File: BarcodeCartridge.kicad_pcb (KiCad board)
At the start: 2 copper layers, 64.8 x 55.9 mm, 3 parts, among them J1 Cartridge Connector, U1 W25Q128

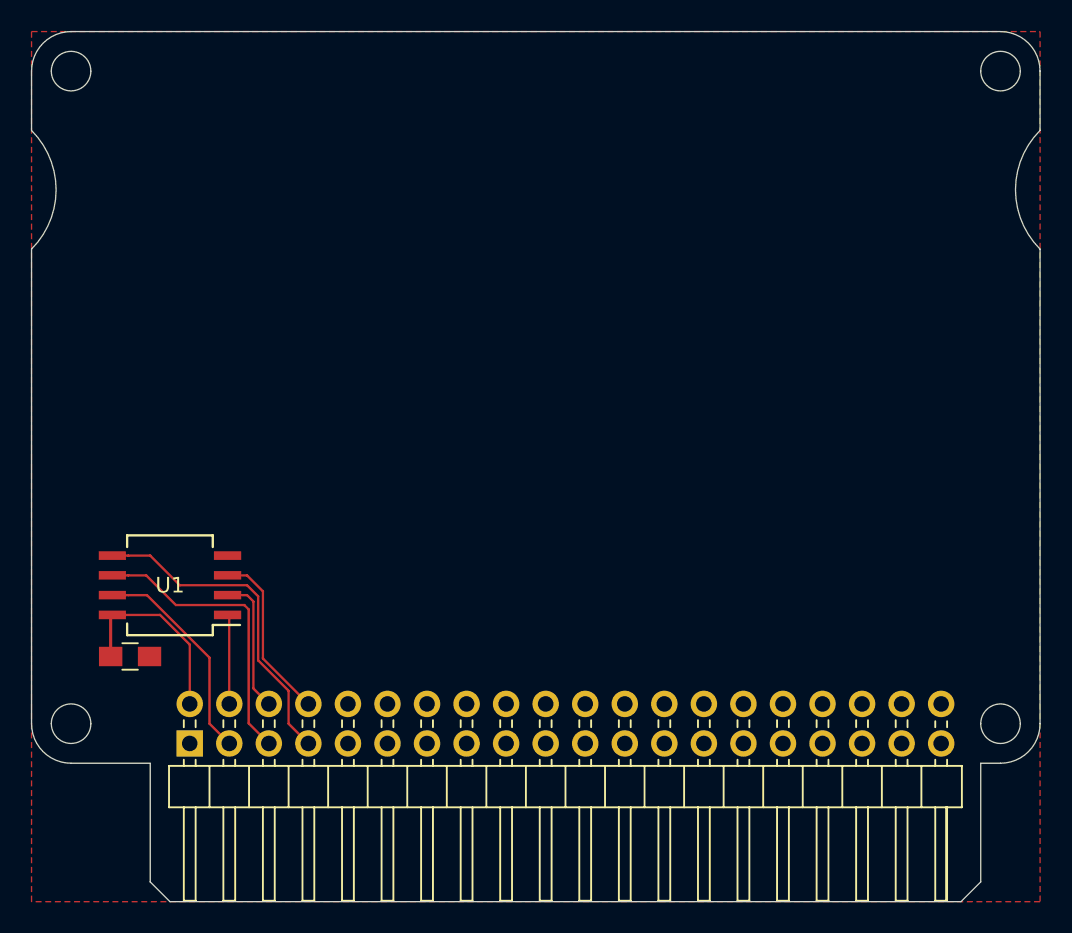
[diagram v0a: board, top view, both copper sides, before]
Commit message: First design of the Barcode reader cartridge
Also updated:
- README
- Render image
- .gitignore
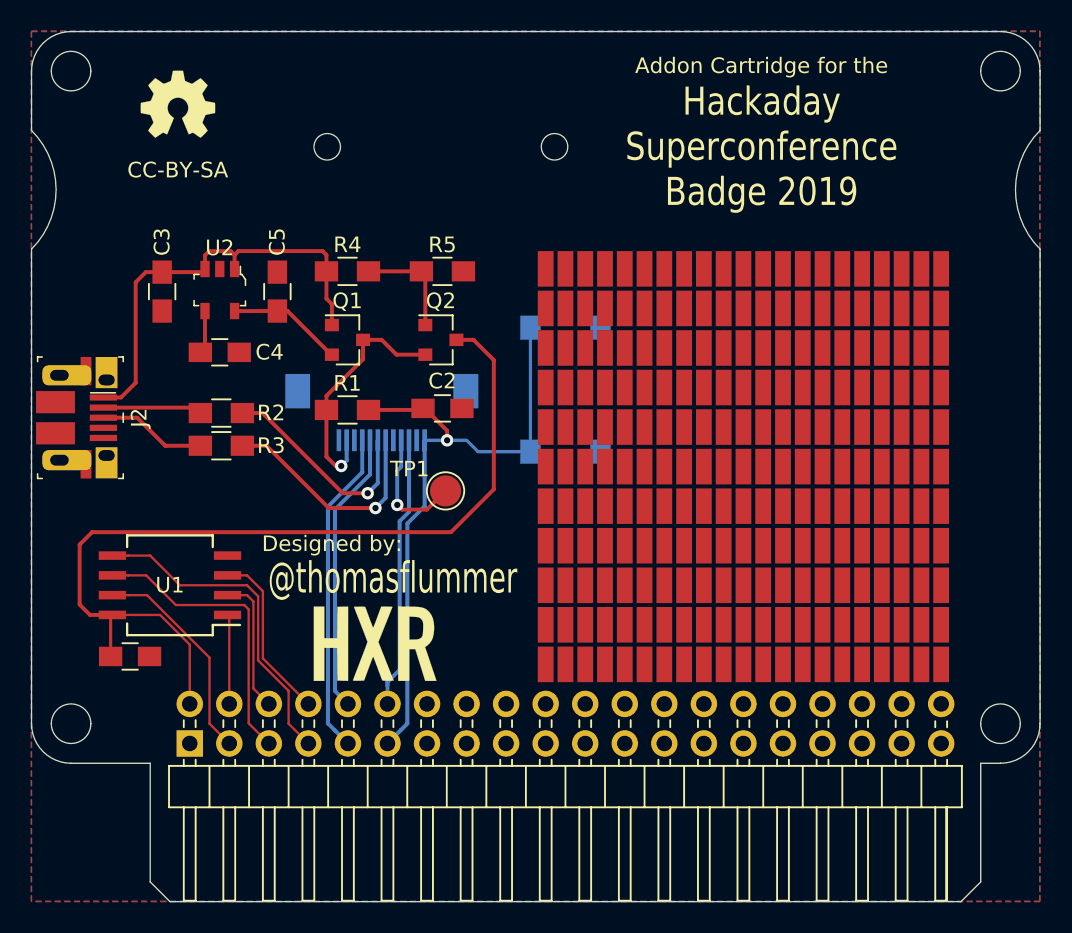
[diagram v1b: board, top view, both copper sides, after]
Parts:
- added C2: 0.1uF, Capacitors_SMD:C_0805_HandSoldering, F.Cu at (93.7, 75.0)
- added C3: 1uF, Capacitors_SMD:C_0805_HandSoldering, F.Cu at (75.7, 67.5)
- added C4: 0.1uF, Capacitors_SMD:C_0805_HandSoldering, F.Cu at (79.4, 71.4)
- added C5: 2.2uF, Capacitors_SMD:C_0805_HandSoldering, F.Cu at (83.1, 67.5)
- added G***: LOGO, Aesthetics:oshw_logo_5.0mm, F.Cu at (76.7, 55.5)
- added G***: LOGO, Aesthetics:HXR_logo_small, F.Cu at (92.1, 90.1)
- added J2: 10103594-0001LF, digikey-footprints:USB_Micro_B_Female_10103594-0001LF, F.Cu at (69.1, 75.6)
- added M1: GM65-S, SuperconCartridge:SD-52892-044, B.Cu at (89.8, 75.0)
- added Q1: SMD-MOSFET-N-CH-20V-2.1A-CJ2302_SOT-23_, TO_SOT_Packages_SMD:SOT-23, F.Cu at (87.6, 70.6)
- added Q2: SMD-MOSFET-P-CH-8V-4.1A-CJ2305_SOT-23_, TO_SOT_Packages_SMD:SOT-23, F.Cu at (93.6, 70.6)
- added R1: 4.7k, Resistors_SMD:R_0805_HandSoldering, F.Cu at (87.6, 75.1)
- added R2: 22, Resistors_SMD:R_0805_HandSoldering, F.Cu at (79.5, 75.3)
- added R3: 22, Resistors_SMD:R_0805_HandSoldering, F.Cu at (79.5, 77.4)
- added R4: 4.7k, Resistors_SMD:R_0805_HandSoldering, F.Cu at (87.6, 66.2)
- added R5: 6.8k, Resistors_SMD:R_0805_HandSoldering, F.Cu at (93.7, 66.2)
- added READER MODULE: GM65-S, SuperconCartridge:GM65-S, B.Cu at (93.6, 50.8)
- added REF**: SMD Proto pad, Connectors:SMD_Proto_pad, F.Cu at (124.5, 66.0)
- added REF**: SMD Proto pad, Connectors:SMD_Proto_pad, F.Cu at (102.9, 66.0)
- added REF**: SMD Proto pad, Connectors:SMD_Proto_pad, F.Cu at (121.9, 76.2)
- added REF**: SMD Proto pad, Connectors:SMD_Proto_pad, F.Cu at (108.0, 76.2)
- added REF**: SMD Proto pad, Connectors:SMD_Proto_pad, F.Cu at (101.6, 76.2)
- added REF**: SMD Proto pad, Connectors:SMD_Proto_pad, F.Cu at (118.1, 76.2)
- added REF**: SMD Proto pad, Connectors:SMD_Proto_pad, F.Cu at (125.7, 76.2)
- added REF**: SMD Proto pad, Connectors:SMD_Proto_pad, F.Cu at (123.2, 76.2)
- added REF**: SMD Proto pad, Connectors:SMD_Proto_pad, F.Cu at (124.5, 78.7)
- added REF**: SMD Proto pad, Connectors:SMD_Proto_pad, F.Cu at (105.4, 78.7)
- added REF**: SMD Proto pad, Connectors:SMD_Proto_pad, F.Cu at (100.3, 78.7)
- added REF**: SMD Proto pad, Connectors:SMD_Proto_pad, F.Cu at (116.8, 78.7)
- added REF**: SMD Proto pad, Connectors:SMD_Proto_pad, F.Cu at (111.8, 66.0)
- added REF**: SMD Proto pad, Connectors:SMD_Proto_pad, F.Cu at (102.9, 78.7)
- added REF**: SMD Proto pad, Connectors:SMD_Proto_pad, F.Cu at (114.3, 78.7)
- added REF**: SMD Proto pad, Connectors:SMD_Proto_pad, F.Cu at (104.1, 78.7)
- added REF**: SMD Proto pad, Connectors:SMD_Proto_pad, F.Cu at (106.7, 78.7)
- added REF**: SMD Proto pad, Connectors:SMD_Proto_pad, F.Cu at (113.0, 78.7)
- added REF**: SMD Proto pad, Connectors:SMD_Proto_pad, F.Cu at (119.4, 78.7)
- added REF**: SMD Proto pad, Connectors:SMD_Proto_pad, F.Cu at (120.7, 78.7)
- added REF**: SMD Proto pad, Connectors:SMD_Proto_pad, F.Cu at (115.6, 78.7)
- added REF**: SMD Proto pad, Connectors:SMD_Proto_pad, F.Cu at (110.5, 78.7)
- added REF**: SMD Proto pad, Connectors:SMD_Proto_pad, F.Cu at (111.8, 78.7)
- added REF**: SMD Proto pad, Connectors:SMD_Proto_pad, F.Cu at (109.2, 66.0)
- added REF**: SMD Proto pad, Connectors:SMD_Proto_pad, F.Cu at (109.2, 78.7)
- added REF**: SMD Proto pad, Connectors:SMD_Proto_pad, F.Cu at (121.9, 78.7)
- added REF**: SMD Proto pad, Connectors:SMD_Proto_pad, F.Cu at (108.0, 78.7)
- added REF**: SMD Proto pad, Connectors:SMD_Proto_pad, F.Cu at (101.6, 78.7)
- added REF**: SMD Proto pad, Connectors:SMD_Proto_pad, F.Cu at (118.1, 78.7)
- added REF**: SMD Proto pad, Connectors:SMD_Proto_pad, F.Cu at (125.7, 78.7)
- added REF**: SMD Proto pad, Connectors:SMD_Proto_pad, F.Cu at (123.2, 78.7)
- added REF**: SMD Proto pad, Connectors:SMD_Proto_pad, F.Cu at (124.5, 81.3)
- added REF**: SMD Proto pad, Connectors:SMD_Proto_pad, F.Cu at (105.4, 81.3)
- added REF**: SMD Proto pad, Connectors:SMD_Proto_pad, F.Cu at (100.3, 81.3)
- added REF**: SMD Proto pad, Connectors:SMD_Proto_pad, F.Cu at (114.3, 66.0)
- added REF**: SMD Proto pad, Connectors:SMD_Proto_pad, F.Cu at (116.8, 81.3)
- added REF**: SMD Proto pad, Connectors:SMD_Proto_pad, F.Cu at (102.9, 81.3)
- added REF**: SMD Proto pad, Connectors:SMD_Proto_pad, F.Cu at (114.3, 81.3)
- added REF**: SMD Proto pad, Connectors:SMD_Proto_pad, F.Cu at (104.1, 81.3)
- added REF**: SMD Proto pad, Connectors:SMD_Proto_pad, F.Cu at (106.7, 81.3)
- added REF**: SMD Proto pad, Connectors:SMD_Proto_pad, F.Cu at (113.0, 81.3)
- added REF**: SMD Proto pad, Connectors:SMD_Proto_pad, F.Cu at (119.4, 81.3)
- added REF**: SMD Proto pad, Connectors:SMD_Proto_pad, F.Cu at (120.7, 81.3)
- added REF**: SMD Proto pad, Connectors:SMD_Proto_pad, F.Cu at (115.6, 81.3)
- added REF**: SMD Proto pad, Connectors:SMD_Proto_pad, F.Cu at (110.5, 81.3)
- added REF**: SMD Proto pad, Connectors:SMD_Proto_pad, F.Cu at (104.1, 66.0)
- added REF**: SMD Proto pad, Connectors:SMD_Proto_pad, F.Cu at (111.8, 81.3)
- added REF**: SMD Proto pad, Connectors:SMD_Proto_pad, F.Cu at (109.2, 81.3)
- added REF**: SMD Proto pad, Connectors:SMD_Proto_pad, F.Cu at (121.9, 81.3)
- added REF**: SMD Proto pad, Connectors:SMD_Proto_pad, F.Cu at (108.0, 81.3)
- added REF**: SMD Proto pad, Connectors:SMD_Proto_pad, F.Cu at (101.6, 81.3)
- added REF**: SMD Proto pad, Connectors:SMD_Proto_pad, F.Cu at (118.1, 81.3)
- added REF**: SMD Proto pad, Connectors:SMD_Proto_pad, F.Cu at (125.7, 81.3)
- added REF**: SMD Proto pad, Connectors:SMD_Proto_pad, F.Cu at (123.2, 81.3)
- added REF**: SMD Proto pad, Connectors:SMD_Proto_pad, F.Cu at (123.2, 83.8)
- added REF**: SMD Proto pad, Connectors:SMD_Proto_pad, F.Cu at (118.1, 83.8)
- added REF**: SMD Proto pad, Connectors:SMD_Proto_pad, F.Cu at (106.7, 66.0)
- added REF**: SMD Proto pad, Connectors:SMD_Proto_pad, F.Cu at (125.7, 83.8)
- added REF**: SMD Proto pad, Connectors:SMD_Proto_pad, F.Cu at (120.7, 83.8)
- added REF**: SMD Proto pad, Connectors:SMD_Proto_pad, F.Cu at (115.6, 83.8)
- added REF**: SMD Proto pad, Connectors:SMD_Proto_pad, F.Cu at (110.5, 83.8)
- added REF**: SMD Proto pad, Connectors:SMD_Proto_pad, F.Cu at (111.8, 83.8)
- added REF**: SMD Proto pad, Connectors:SMD_Proto_pad, F.Cu at (109.2, 83.8)
- added REF**: SMD Proto pad, Connectors:SMD_Proto_pad, F.Cu at (119.4, 83.8)
- added REF**: SMD Proto pad, Connectors:SMD_Proto_pad, F.Cu at (104.1, 83.8)
- added REF**: SMD Proto pad, Connectors:SMD_Proto_pad, F.Cu at (106.7, 83.8)
- added REF**: SMD Proto pad, Connectors:SMD_Proto_pad, F.Cu at (113.0, 83.8)
- added REF**: SMD Proto pad, Connectors:SMD_Proto_pad, F.Cu at (113.0, 66.0)
- added REF**: SMD Proto pad, Connectors:SMD_Proto_pad, F.Cu at (100.3, 83.8)
- added REF**: SMD Proto pad, Connectors:SMD_Proto_pad, F.Cu at (116.8, 83.8)
- added REF**: SMD Proto pad, Connectors:SMD_Proto_pad, F.Cu at (102.9, 83.8)
- added REF**: SMD Proto pad, Connectors:SMD_Proto_pad, F.Cu at (114.3, 83.8)
- added REF**: SMD Proto pad, Connectors:SMD_Proto_pad, F.Cu at (124.5, 83.8)
- added REF**: SMD Proto pad, Connectors:SMD_Proto_pad, F.Cu at (105.4, 83.8)
- added REF**: SMD Proto pad, Connectors:SMD_Proto_pad, F.Cu at (121.9, 83.8)
- added REF**: SMD Proto pad, Connectors:SMD_Proto_pad, F.Cu at (108.0, 83.8)
- added REF**: SMD Proto pad, Connectors:SMD_Proto_pad, F.Cu at (101.6, 83.8)
- added REF**: SMD Proto pad, Connectors:SMD_Proto_pad, F.Cu at (123.2, 86.4)
- added REF**: SMD Proto pad, Connectors:SMD_Proto_pad, F.Cu at (119.4, 66.0)
- added REF**: SMD Proto pad, Connectors:SMD_Proto_pad, F.Cu at (108.0, 86.4)
- added REF**: SMD Proto pad, Connectors:SMD_Proto_pad, F.Cu at (116.8, 86.4)
- added REF**: SMD Proto pad, Connectors:SMD_Proto_pad, F.Cu at (104.1, 86.4)
- added REF**: SMD Proto pad, Connectors:SMD_Proto_pad, F.Cu at (106.7, 86.4)
- added REF**: SMD Proto pad, Connectors:SMD_Proto_pad, F.Cu at (113.0, 86.4)
- added REF**: SMD Proto pad, Connectors:SMD_Proto_pad, F.Cu at (100.3, 86.4)
- added REF**: SMD Proto pad, Connectors:SMD_Proto_pad, F.Cu at (102.9, 86.4)
- added REF**: SMD Proto pad, Connectors:SMD_Proto_pad, F.Cu at (114.3, 86.4)
- added REF**: SMD Proto pad, Connectors:SMD_Proto_pad, F.Cu at (124.5, 86.4)
- added REF**: SMD Proto pad, Connectors:SMD_Proto_pad, F.Cu at (105.4, 86.4)
- added REF**: SMD Proto pad, Connectors:SMD_Proto_pad, F.Cu at (120.7, 66.0)
- added REF**: SMD Proto pad, Connectors:SMD_Proto_pad, F.Cu at (118.1, 86.4)
- added REF**: SMD Proto pad, Connectors:SMD_Proto_pad, F.Cu at (125.7, 86.4)
- added REF**: SMD Proto pad, Connectors:SMD_Proto_pad, F.Cu at (120.7, 86.4)
- added REF**: SMD Proto pad, Connectors:SMD_Proto_pad, F.Cu at (115.6, 86.4)
- added REF**: SMD Proto pad, Connectors:SMD_Proto_pad, F.Cu at (121.9, 86.4)
- added REF**: SMD Proto pad, Connectors:SMD_Proto_pad, F.Cu at (110.5, 86.4)
- added REF**: SMD Proto pad, Connectors:SMD_Proto_pad, F.Cu at (111.8, 86.4)
- added REF**: SMD Proto pad, Connectors:SMD_Proto_pad, F.Cu at (109.2, 86.4)
- added REF**: SMD Proto pad, Connectors:SMD_Proto_pad, F.Cu at (119.4, 86.4)
- added REF**: SMD Proto pad, Connectors:SMD_Proto_pad, F.Cu at (101.6, 86.4)
- added REF**: SMD Proto pad, Connectors:SMD_Proto_pad, F.Cu at (115.6, 66.0)
- added REF**: SMD Proto pad, Connectors:SMD_Proto_pad, F.Cu at (110.5, 88.9)
- added REF**: SMD Proto pad, Connectors:SMD_Proto_pad, F.Cu at (125.7, 88.9)
- added REF**: SMD Proto pad, Connectors:SMD_Proto_pad, F.Cu at (120.7, 88.9)
- added REF**: SMD Proto pad, Connectors:SMD_Proto_pad, F.Cu at (115.6, 88.9)
- added REF**: SMD Proto pad, Connectors:SMD_Proto_pad, F.Cu at (111.8, 88.9)
- added REF**: SMD Proto pad, Connectors:SMD_Proto_pad, F.Cu at (121.9, 88.9)
- added REF**: SMD Proto pad, Connectors:SMD_Proto_pad, F.Cu at (123.2, 88.9)
- added REF**: SMD Proto pad, Connectors:SMD_Proto_pad, F.Cu at (114.3, 88.9)
- added REF**: SMD Proto pad, Connectors:SMD_Proto_pad, F.Cu at (102.9, 88.9)
- added REF**: SMD Proto pad, Connectors:SMD_Proto_pad, F.Cu at (108.0, 88.9)
- added REF**: SMD Proto pad, Connectors:SMD_Proto_pad, F.Cu at (105.4, 66.0)
- added REF**: SMD Proto pad, Connectors:SMD_Proto_pad, F.Cu at (110.5, 66.0)
- added REF**: SMD Proto pad, Connectors:SMD_Proto_pad, F.Cu at (116.8, 88.9)
- added REF**: SMD Proto pad, Connectors:SMD_Proto_pad, F.Cu at (104.1, 88.9)
- added REF**: SMD Proto pad, Connectors:SMD_Proto_pad, F.Cu at (106.7, 88.9)
- added REF**: SMD Proto pad, Connectors:SMD_Proto_pad, F.Cu at (113.0, 88.9)
- added REF**: SMD Proto pad, Connectors:SMD_Proto_pad, F.Cu at (100.3, 88.9)
- added REF**: SMD Proto pad, Connectors:SMD_Proto_pad, F.Cu at (119.4, 88.9)
- added REF**: SMD Proto pad, Connectors:SMD_Proto_pad, F.Cu at (101.6, 88.9)
- added REF**: SMD Proto pad, Connectors:SMD_Proto_pad, F.Cu at (109.2, 88.9)
- added REF**: SMD Proto pad, Connectors:SMD_Proto_pad, F.Cu at (105.4, 88.9)
- added REF**: SMD Proto pad, Connectors:SMD_Proto_pad, F.Cu at (118.1, 88.9)
- added REF**: SMD Proto pad, Connectors:SMD_Proto_pad, F.Cu at (123.2, 66.0)
- added REF**: SMD Proto pad, Connectors:SMD_Proto_pad, F.Cu at (124.5, 88.9)
- added REF**: SMD Proto pad, Connectors:SMD_Proto_pad, F.Cu at (125.7, 91.4)
- added REF**: SMD Proto pad, Connectors:SMD_Proto_pad, F.Cu at (124.5, 91.4)
- added REF**: SMD Proto pad, Connectors:SMD_Proto_pad, F.Cu at (123.2, 91.4)
- added REF**: SMD Proto pad, Connectors:SMD_Proto_pad, F.Cu at (121.9, 91.4)
- added REF**: SMD Proto pad, Connectors:SMD_Proto_pad, F.Cu at (120.7, 91.4)
- added REF**: SMD Proto pad, Connectors:SMD_Proto_pad, F.Cu at (119.4, 91.4)
- added REF**: SMD Proto pad, Connectors:SMD_Proto_pad, F.Cu at (118.1, 91.4)
- added REF**: SMD Proto pad, Connectors:SMD_Proto_pad, F.Cu at (116.8, 91.4)
- added REF**: SMD Proto pad, Connectors:SMD_Proto_pad, F.Cu at (115.6, 91.4)
- added REF**: SMD Proto pad, Connectors:SMD_Proto_pad, F.Cu at (124.5, 68.6)
- added REF**: SMD Proto pad, Connectors:SMD_Proto_pad, F.Cu at (114.3, 91.4)
- added REF**: SMD Proto pad, Connectors:SMD_Proto_pad, F.Cu at (113.0, 91.4)
- added REF**: SMD Proto pad, Connectors:SMD_Proto_pad, F.Cu at (111.8, 91.4)
- added REF**: SMD Proto pad, Connectors:SMD_Proto_pad, F.Cu at (110.5, 91.4)
- added REF**: SMD Proto pad, Connectors:SMD_Proto_pad, F.Cu at (109.2, 91.4)
- added REF**: SMD Proto pad, Connectors:SMD_Proto_pad, F.Cu at (108.0, 91.4)
- added REF**: SMD Proto pad, Connectors:SMD_Proto_pad, F.Cu at (106.7, 91.4)
- added REF**: SMD Proto pad, Connectors:SMD_Proto_pad, F.Cu at (105.4, 91.4)
- added REF**: SMD Proto pad, Connectors:SMD_Proto_pad, F.Cu at (104.1, 91.4)
- added REF**: SMD Proto pad, Connectors:SMD_Proto_pad, F.Cu at (102.9, 91.4)
- added REF**: SMD Proto pad, Connectors:SMD_Proto_pad, F.Cu at (105.4, 68.6)
- added REF**: SMD Proto pad, Connectors:SMD_Proto_pad, F.Cu at (101.6, 91.4)
- added REF**: SMD Proto pad, Connectors:SMD_Proto_pad, F.Cu at (100.3, 91.4)
- added REF**: SMD Proto pad, Connectors:SMD_Proto_pad, F.Cu at (121.9, 68.6)
- added REF**: SMD Proto pad, Connectors:SMD_Proto_pad, F.Cu at (108.0, 68.6)
- added REF**: SMD Proto pad, Connectors:SMD_Proto_pad, F.Cu at (101.6, 68.6)
- added REF**: SMD Proto pad, Connectors:SMD_Proto_pad, F.Cu at (118.1, 68.6)
- added REF**: SMD Proto pad, Connectors:SMD_Proto_pad, F.Cu at (125.7, 68.6)
- added REF**: SMD Proto pad, Connectors:SMD_Proto_pad, F.Cu at (100.3, 68.6)
- added REF**: SMD Proto pad, Connectors:SMD_Proto_pad, F.Cu at (121.9, 66.0)
- added REF**: SMD Proto pad, Connectors:SMD_Proto_pad, F.Cu at (116.8, 68.6)
- added REF**: SMD Proto pad, Connectors:SMD_Proto_pad, F.Cu at (102.9, 68.6)
- added REF**: SMD Proto pad, Connectors:SMD_Proto_pad, F.Cu at (111.8, 68.6)
- added REF**: SMD Proto pad, Connectors:SMD_Proto_pad, F.Cu at (109.2, 68.6)
- added REF**: SMD Proto pad, Connectors:SMD_Proto_pad, F.Cu at (114.3, 68.6)
- added REF**: SMD Proto pad, Connectors:SMD_Proto_pad, F.Cu at (104.1, 68.6)
- added REF**: SMD Proto pad, Connectors:SMD_Proto_pad, F.Cu at (106.7, 68.6)
- added REF**: SMD Proto pad, Connectors:SMD_Proto_pad, F.Cu at (113.0, 68.6)
- added REF**: SMD Proto pad, Connectors:SMD_Proto_pad, F.Cu at (119.4, 68.6)
- added REF**: SMD Proto pad, Connectors:SMD_Proto_pad, F.Cu at (120.7, 68.6)
- added REF**: SMD Proto pad, Connectors:SMD_Proto_pad, F.Cu at (108.0, 66.0)
- added REF**: SMD Proto pad, Connectors:SMD_Proto_pad, F.Cu at (115.6, 68.6)
- added REF**: SMD Proto pad, Connectors:SMD_Proto_pad, F.Cu at (110.5, 68.6)
- added REF**: SMD Proto pad, Connectors:SMD_Proto_pad, F.Cu at (123.2, 68.6)
- added REF**: SMD Proto pad, Connectors:SMD_Proto_pad, F.Cu at (124.5, 71.1)
- added REF**: SMD Proto pad, Connectors:SMD_Proto_pad, F.Cu at (105.4, 71.1)
- added REF**: SMD Proto pad, Connectors:SMD_Proto_pad, F.Cu at (121.9, 71.1)
- added REF**: SMD Proto pad, Connectors:SMD_Proto_pad, F.Cu at (108.0, 71.1)
- added REF**: SMD Proto pad, Connectors:SMD_Proto_pad, F.Cu at (101.6, 71.1)
- added REF**: SMD Proto pad, Connectors:SMD_Proto_pad, F.Cu at (118.1, 71.1)
- added REF**: SMD Proto pad, Connectors:SMD_Proto_pad, F.Cu at (125.7, 71.1)
- added REF**: SMD Proto pad, Connectors:SMD_Proto_pad, F.Cu at (101.6, 66.0)
- added REF**: SMD Proto pad, Connectors:SMD_Proto_pad, F.Cu at (100.3, 71.1)
- added REF**: SMD Proto pad, Connectors:SMD_Proto_pad, F.Cu at (116.8, 71.1)
- added REF**: SMD Proto pad, Connectors:SMD_Proto_pad, F.Cu at (102.9, 71.1)
- added REF**: SMD Proto pad, Connectors:SMD_Proto_pad, F.Cu at (111.8, 71.1)
- added REF**: SMD Proto pad, Connectors:SMD_Proto_pad, F.Cu at (109.2, 71.1)
- added REF**: SMD Proto pad, Connectors:SMD_Proto_pad, F.Cu at (114.3, 71.1)
- added REF**: SMD Proto pad, Connectors:SMD_Proto_pad, F.Cu at (104.1, 71.1)
- added REF**: SMD Proto pad, Connectors:SMD_Proto_pad, F.Cu at (106.7, 71.1)
- added REF**: SMD Proto pad, Connectors:SMD_Proto_pad, F.Cu at (113.0, 71.1)
- added REF**: SMD Proto pad, Connectors:SMD_Proto_pad, F.Cu at (119.4, 71.1)
- added REF**: SMD Proto pad, Connectors:SMD_Proto_pad, F.Cu at (118.1, 66.0)
- added REF**: SMD Proto pad, Connectors:SMD_Proto_pad, F.Cu at (120.7, 71.1)
- added REF**: SMD Proto pad, Connectors:SMD_Proto_pad, F.Cu at (115.6, 71.1)
- added REF**: SMD Proto pad, Connectors:SMD_Proto_pad, F.Cu at (110.5, 71.1)
- added REF**: SMD Proto pad, Connectors:SMD_Proto_pad, F.Cu at (123.2, 71.1)
- added REF**: SMD Proto pad, Connectors:SMD_Proto_pad, F.Cu at (124.5, 73.7)
- added REF**: SMD Proto pad, Connectors:SMD_Proto_pad, F.Cu at (105.4, 73.7)
- added REF**: SMD Proto pad, Connectors:SMD_Proto_pad, F.Cu at (121.9, 73.7)
- added REF**: SMD Proto pad, Connectors:SMD_Proto_pad, F.Cu at (108.0, 73.7)
- added REF**: SMD Proto pad, Connectors:SMD_Proto_pad, F.Cu at (101.6, 73.7)
- added REF**: SMD Proto pad, Connectors:SMD_Proto_pad, F.Cu at (118.1, 73.7)
- added REF**: SMD Proto pad, Connectors:SMD_Proto_pad, F.Cu at (125.7, 66.0)
- added REF**: SMD Proto pad, Connectors:SMD_Proto_pad, F.Cu at (125.7, 73.7)
- added REF**: SMD Proto pad, Connectors:SMD_Proto_pad, F.Cu at (100.3, 73.7)
- added REF**: SMD Proto pad, Connectors:SMD_Proto_pad, F.Cu at (116.8, 73.7)
- added REF**: SMD Proto pad, Connectors:SMD_Proto_pad, F.Cu at (102.9, 73.7)
- added REF**: SMD Proto pad, Connectors:SMD_Proto_pad, F.Cu at (111.8, 73.7)
- added REF**: SMD Proto pad, Connectors:SMD_Proto_pad, F.Cu at (109.2, 73.7)
- added REF**: SMD Proto pad, Connectors:SMD_Proto_pad, F.Cu at (114.3, 73.7)
- added REF**: SMD Proto pad, Connectors:SMD_Proto_pad, F.Cu at (104.1, 73.7)
- added REF**: SMD Proto pad, Connectors:SMD_Proto_pad, F.Cu at (106.7, 73.7)
- added REF**: SMD Proto pad, Connectors:SMD_Proto_pad, F.Cu at (113.0, 73.7)
- added REF**: SMD Proto pad, Connectors:SMD_Proto_pad, F.Cu at (100.3, 66.0)
- added REF**: SMD Proto pad, Connectors:SMD_Proto_pad, F.Cu at (119.4, 73.7)
- added REF**: SMD Proto pad, Connectors:SMD_Proto_pad, F.Cu at (120.7, 73.7)
- added REF**: SMD Proto pad, Connectors:SMD_Proto_pad, F.Cu at (115.6, 73.7)
- added REF**: SMD Proto pad, Connectors:SMD_Proto_pad, F.Cu at (110.5, 73.7)
- added REF**: SMD Proto pad, Connectors:SMD_Proto_pad, F.Cu at (123.2, 73.7)
- added REF**: SMD Proto pad, Connectors:SMD_Proto_pad, F.Cu at (124.5, 76.2)
- added REF**: SMD Proto pad, Connectors:SMD_Proto_pad, F.Cu at (105.4, 76.2)
- added REF**: SMD Proto pad, Connectors:SMD_Proto_pad, F.Cu at (100.3, 76.2)
- added REF**: SMD Proto pad, Connectors:SMD_Proto_pad, F.Cu at (116.8, 76.2)
- added REF**: SMD Proto pad, Connectors:SMD_Proto_pad, F.Cu at (102.9, 76.2)
- added REF**: SMD Proto pad, Connectors:SMD_Proto_pad, F.Cu at (116.8, 66.0)
- added REF**: SMD Proto pad, Connectors:SMD_Proto_pad, F.Cu at (114.3, 76.2)
- added REF**: SMD Proto pad, Connectors:SMD_Proto_pad, F.Cu at (104.1, 76.2)
- added REF**: SMD Proto pad, Connectors:SMD_Proto_pad, F.Cu at (106.7, 76.2)
- added REF**: SMD Proto pad, Connectors:SMD_Proto_pad, F.Cu at (113.0, 76.2)
- added REF**: SMD Proto pad, Connectors:SMD_Proto_pad, F.Cu at (119.4, 76.2)
- added REF**: SMD Proto pad, Connectors:SMD_Proto_pad, F.Cu at (120.7, 76.2)
- added REF**: SMD Proto pad, Connectors:SMD_Proto_pad, F.Cu at (115.6, 76.2)
- added REF**: SMD Proto pad, Connectors:SMD_Proto_pad, F.Cu at (110.5, 76.2)
- added REF**: SMD Proto pad, Connectors:SMD_Proto_pad, F.Cu at (111.8, 76.2)
- added REF**: SMD Proto pad, Connectors:SMD_Proto_pad, F.Cu at (109.2, 76.2)
- added SW1: SW_Push, Buttons_Switches_SMD:SW_SPST_PTS645, B.Cu at (101.6, 73.8)
- added TP1: Buzzer, Connectors_TestPoints:Test_Point_Pad_d2.0mm, F.Cu at (93.9, 80.3)
- added U2: LP2985-33DBVR, digikey-footprints:SOT-753, F.Cu at (79.4, 67.4)
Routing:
- net +3V3: track 12.3 -> 57.8 mm
- net GENIO3: track 0.00 -> 41.8 mm, vias 0 -> 1
- net VUSB: track 0.00 -> 28.4 mm
- net GENIO1: track 0.00 -> 20.9 mm
- net GENIO2: track 0.00 -> 18.2 mm
- net GENIO4: track 0.00 -> 17.5 mm
- net VCC: track 0.00 -> 15.9 mm, vias 0 -> 1
- net Net-(M1-Pad7): track 0.00 -> 14.8 mm, vias 0 -> 1
- net Net-(M1-Pad6): track 0.00 -> 13.9 mm, vias 0 -> 1
- net Net-(M1-Pad9): track 0.00 -> 7.97 mm, vias 0 -> 1
- net Net-(C5-Pad1): track 0.00 -> 7.41 mm
- net D+: track 0.00 -> 6.97 mm
- net Net-(Q2-Pad1): track 0.00 -> 6.95 mm
- net D-: track 0.00 -> 6.37 mm
- net Net-(C4-Pad1): track 0.00 -> 2.77 mm
- added copper zone on B.Cu, net GND
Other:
- net class Default: clearance 0.2 -> 0.15
- rule trace_clearance: 0.2 -> 0.15
- rule trace_min: 0.2 -> 0.15
- board text added: "@thomasflummer"
- board text added: "Addon Cartridge for the"
- board text added: "BARCODE SCANNER"
- board text added: "CC-BY-SA"
- board text added: "Designed by:"
- board text added: "Hackaday Superconference Badge 2019"
